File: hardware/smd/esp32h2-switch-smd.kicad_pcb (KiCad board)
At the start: 2 copper layers, 0 parts

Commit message: Complete PCB and schematics after fucking a lot of iterations
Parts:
- added AE1: Antenna_Chip, KiCadX_Antennas_SMD:PCB_antenna_Espressif_2.4GHz_right, F.Cu at (150.5, 112.7)
- added C1: 22u 10V, Capacitor_THT:CP_Radial_D4.0mm_P1.50mm, F.Cu at (162.1, 106.8)
- added C10: 100n 10V X7R, Capacitor_SMD:C_0402_1005Metric, B.Cu at (158.7, 104.3)
- added C11: 100n 35V X7R, Capacitor_SMD:C_0603_1608Metric, B.Cu at (170.0, 96.7)
- added C12: 1n 10V X7R, Capacitor_SMD:C_0402_1005Metric, B.Cu at (158.7, 105.3)
- added C13: 2.2n 35V X7R, Capacitor_SMD:C_0402_1005Metric, B.Cu at (168.7, 93.6)
- added C14: 100n 10V X7R, Capacitor_SMD:C_0402_1005Metric, F.Cu at (156.5, 104.5)
- added C15: 5.6p C0G, Capacitor_SMD:C_0201_0603Metric, F.Cu at (155.1, 108.1)
- added C16: 100n 10V X7R, Capacitor_SMD:C_0402_1005Metric, F.Cu at (156.5, 101.3)
- added C17: 8p 10V C0G, Capacitor_SMD:C_0201_0603Metric, F.Cu at (154.2, 108.2)
- added C18: 2.2p C0G, Capacitor_SMD:C_0201_0603Metric, F.Cu at (155.5, 109.1)
- added C19: 100n 10V X7R, Capacitor_SMD:C_0402_1005Metric, F.Cu at (150.4, 102.2)
- added C2: 100n 10V X7R, Capacitor_SMD:C_0402_1005Metric, F.Cu at (169.9, 105.8)
- added C20: 100n 10V X7R, Capacitor_SMD:C_0402_1005Metric, F.Cu at (152.2, 105.8)
- added C21: 8p 10V C0G, Capacitor_SMD:C_0201_0603Metric, F.Cu at (150.9, 107.4)
- added C22: 100n 10V X7R, Capacitor_SMD:C_0402_1005Metric, F.Cu at (154.3, 106.2)
- added C3: 220n 275V X2, Capacitor_THT:C_Rect_L13.0mm_W6.0mm_P10.00mm_FKS3_FKP3_MKS4, F.Cu at (144.9, 94.8)
- added C4: 4.7u 400V, Capacitor_THT:CP_Radial_D6.3mm_P2.50mm, F.Cu at (164.7, 84.8)
- added C5: 22u 10V, Capacitor_THT:CP_Radial_D4.0mm_P1.50mm, F.Cu at (172.7, 106.9)
- added C6: 100n 10V X7R, Capacitor_SMD:C_0402_1005Metric, F.Cu at (169.9, 107.9)
- added C7: 2.2n 50V X7R, Capacitor_SMD:C_0402_1005Metric, B.Cu at (167.6, 98.1)
- added C8: 470u 10V, KiCadX_Capacitors_THT:CP_Radial_D6.0mm_P2.50mm, F.Cu at (159.1, 84.8)
- added C9: 22u 35V, Capacitor_THT:CP_Radial_D5.0mm_P2.00mm, F.Cu at (173.2, 85.1)
- added D1: 1A 600V, Package_TO_SOT_SMD:TO-269AA, B.Cu at (149.7, 89.5)
- added D2: 40V 1A, Diode_SMD:D_SOD-323, B.Cu at (170.2, 93.6)
- added D3: 40V 1A, Diode_SMD:D_SOD-323, B.Cu at (158.7, 102.2)
- added D4: 40V 1A, Diode_SMD:D_SOD-323, B.Cu at (137.1, 108.5)
- added D5: Blue, 3V, 10mA, LED_SMD:LED_0603_1608Metric, F.Cu at (145.5, 107.4)
- added D6: Red, 2V, 10mA, LED_SMD:LED_0603_1608Metric, F.Cu at (144.1, 107.4)
- added F1: T500mA 250V, Fuse:Fuse_Littelfuse_395Series, F.Cu at (124.7, 85.7)
- added FL1: 2×4.7m ≥0.3A ≤2R, KiCadX_Inductors_THT:TDK_B82720K_Vertical_13x9.5mm_P10x7.5mm, F.Cu at (149.0, 86.5)
- added J1: Screw_Terminal_01x02, TerminalBlock_Phoenix:TerminalBlock_Phoenix_PT-1,5-2-5.0-H_1x02_P5.00mm_Horizontal, F.Cu at (127.3, 90.9)
- added J2: Screw_Terminal_01x02, TerminalBlock_Phoenix:TerminalBlock_Phoenix_PT-1,5-2-5.0-H_1x02_P5.00mm_Horizontal, F.Cu at (127.3, 101.9)
- added J5: UART, Connector_PinHeader_1.27mm:PinHeader_1x04_P1.27mm_Vertical, F.Cu at (147.9, 104.0)
- added J6: Conn_01x02_Pin, Connector_PinHeader_1.27mm:PinHeader_1x02_P1.27mm_Vertical, F.Cu at (147.9, 100.4)
- added K1: SPST, 5V 72R, 10A 250VAC, KiCadX_Relays_THT:Relay_SPST_OJ_SH_105HM_000, F.Cu at (136.8, 100.4)
- added L1: 3.9 nH, Inductor_SMD:L_0402_1005Metric, F.Cu at (155.7, 106.9)
- added NT1: NetTie_2, KiCadX_NetTies:NetTie_2_D0.5_P4.0, B.Cu at (128.9, 88.8)
- added NT2: NetTie_2, KiCadX_NetTies:NetTie_2_D0.5_P4.0, B.Cu at (121.7, 97.0)
- added Q1: NPN, 40V, 500mA, Package_TO_SOT_SMD:SOT-323_SC-70, F.Cu at (143.7, 104.2)
- added R1: 30k, Resistor_SMD:R_0402_1005Metric, B.Cu at (168.7, 95.7)
- added R10: 10k, Resistor_SMD:R_0402_1005Metric, F.Cu at (150.4, 100.8)
- added R2: 470R, Resistor_SMD:R_0402_1005Metric, B.Cu at (161.8, 104.8)
- added R3: 10k, Resistor_SMD:R_0402_1005Metric, B.Cu at (163.8, 106.1)
- added R4: 10k, Resistor_SMD:R_0402_1005Metric, B.Cu at (165.6, 106.1)
- added R5: 330R, Resistor_SMD:R_0402_1005Metric, F.Cu at (142.9, 106.9)
- added R6: 220R, Resistor_SMD:R_0402_1005Metric, F.Cu at (145.5, 105.0)
- added R7: 10k, Resistor_SMD:R_0402_1005Metric, F.Cu at (154.7, 99.9)
- added R8: 330R, Resistor_SMD:R_0402_1005Metric, F.Cu at (143.9, 102.1)
- added R9: 10k, Resistor_SMD:R_0402_1005Metric, F.Cu at (145.5, 103.2)
- added RV1: 275V, Varistor:RV_Disc_D9mm_W4.4mm_P5mm, F.Cu at (133.2, 88.7)
- added T1: Wurth 750370423, KiCadX_Transformers_THT:Wurth_750370423_THT_E13, F.Cu at (166.6, 96.5)
- added TH1: 10R 25C, KiCadX_Thermistors_THT:NTC10D_7_Disc_D7.0mm_P5.0mm, F.Cu at (139.5, 86.3)
- added U1: LM1117F-3.3, Package_TO_SOT_SMD:SOT-89-3, F.Cu at (166.6, 107.4)
- added U2: VIPER06, KiCadX_ACDC_Converters_SMD:VIPER06_SSO10, B.Cu at (164.1, 95.2)
- added U3: EL3H7, Package_SO:SSOP-4_4.4x2.6mm_P1.27mm, B.Cu at (167.0, 104.1)
- added U4: TL431, Package_TO_SOT_SMD:SOT-23, B.Cu at (167.5, 107.5)
- added U5: ESP32-H2, KiCadX_MCU_Espressif:TQFN_32_1EP_4x4mm_P0.4mm_EP2.4x2.4mm_Compact, F.Cu at (153.6, 102.8)
- added Y1: 32MHz ±10ppm CL8pF, Crystal:Crystal_SMD_2016-4Pin_2.0x1.6mm, F.Cu at (152.5, 107.8)
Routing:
- net +5V: track 0.00 -> 80.3 mm, vias 0 -> 1
- net N: track 0.00 -> 54.3 mm
- net GND: track 0.00 -> 33.4 mm, vias 0 -> 53
- net L: track 0.00 -> 26.7 mm
- net GND_P: track 0.00 -> 26.4 mm
- net /Power supply/VRECT: track 0.00 -> 25.4 mm
- net /N_IN: track 0.00 -> 17.4 mm
- net Net-(D2-K): track 0.00 -> 17.3 mm
- net L_OUT: track 0.00 -> 15.6 mm
- net +3.3V: track 0.00 -> 15.3 mm, vias 0 -> 16
- net /Control unit/RELAY_CTRL: track 0.00 -> 10.9 mm, vias 0 -> 2
- net /Control unit/RELAY_COIL: track 0.00 -> 9.88 mm
- net Net-(U2-COMP): track 0.00 -> 9.32 mm
- net /Control unit/LED_RUN: track 0.00 -> 8.21 mm, vias 0 -> 2
- net BOOT: track 0.00 -> 7.55 mm
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- added copper zone on In2.Cu, net +3.3V
- added copper zone on B.Cu, net /Power supply/DRAIN
- added copper zone on B.Cu, net GND
- added copper zone on F.Cu, net GND
- added copper zone on In1.Cu, net GND
- added copper zone on B.Cu, net GND_P
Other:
- board outline added: 54.6 x 34.2 mm
- copper layers 2 -> 4

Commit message: Relink symbols and footprints to new lib and fix few errors
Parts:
- AE1: footprint KiCadX_Antennas_SMD:PCB_antenna_Espressif_2.4GHz_right -> PCM_SKC_Antennas_SMD:Antenna_PCB_Espressif_2.4GHz_Right
- C8: footprint KiCadX_Capacitors_THT:CP_Radial_D6.0mm_P2.50mm -> PCM_SKC_Capacitors_THT:CP_Radial_D6.0mm_P2.50mm
- FL1: footprint KiCadX_Inductors_THT:TDK_B82720K_Vertical_13x9.5mm_P10x7.5mm -> PCM_SKC_Inductors_THT:TDK_B82720K_Vertical_13x9.5mm_P10x7.5mm
- K1: footprint KiCadX_Relays_THT:Relay_SPST_OJ_SH_105HM_000 -> PCM_SKC_Relays_THT:OJ_SH_105HM_SPST
- NT1, NT2: footprint KiCadX_NetTies:NetTie_2_D0.5_P4.0 -> PCM_SKC_NetTies:NetTie_2_D0.5_P4.0
- T1: footprint KiCadX_Transformers_THT:Wurth_750370423_THT_E13 -> PCM_SKC_Transformers_THT:Wurth_750370423_THT_E13
- TH1: footprint KiCadX_Thermistors_THT:NTC10D_7_Disc_D7.0mm_P5.0mm -> PCM_SKC_Thermistors_THT:NTC10D_7_Disc_D7.0mm_P5.0mm
- U2: footprint KiCadX_ACDC_Converters_SMD:VIPER06_SSO10 -> PCM_SKC_ACDC_Converters_SMD:STMicroelectronics_VIPER06_SSO10
- U5: footprint KiCadX_MCU_Espressif:TQFN_32_1EP_4x4mm_P0.4mm_EP2.4x2.4mm_Compact -> PCM_SKC_MCU_Espressif:TQFN_32_1EP_4x4mm_P0.4mm_EP2.4x2.4mm_Compact

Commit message: Added logo on silkscreen
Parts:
- added REF**: SIVAKOV_TECH_Circle_Medium_D13.22_1, SIVAKOV.TECH:SIVAKOV_TECH_Circle_Medium_D13.22_1, B.Cu at (135.5, 100.9)

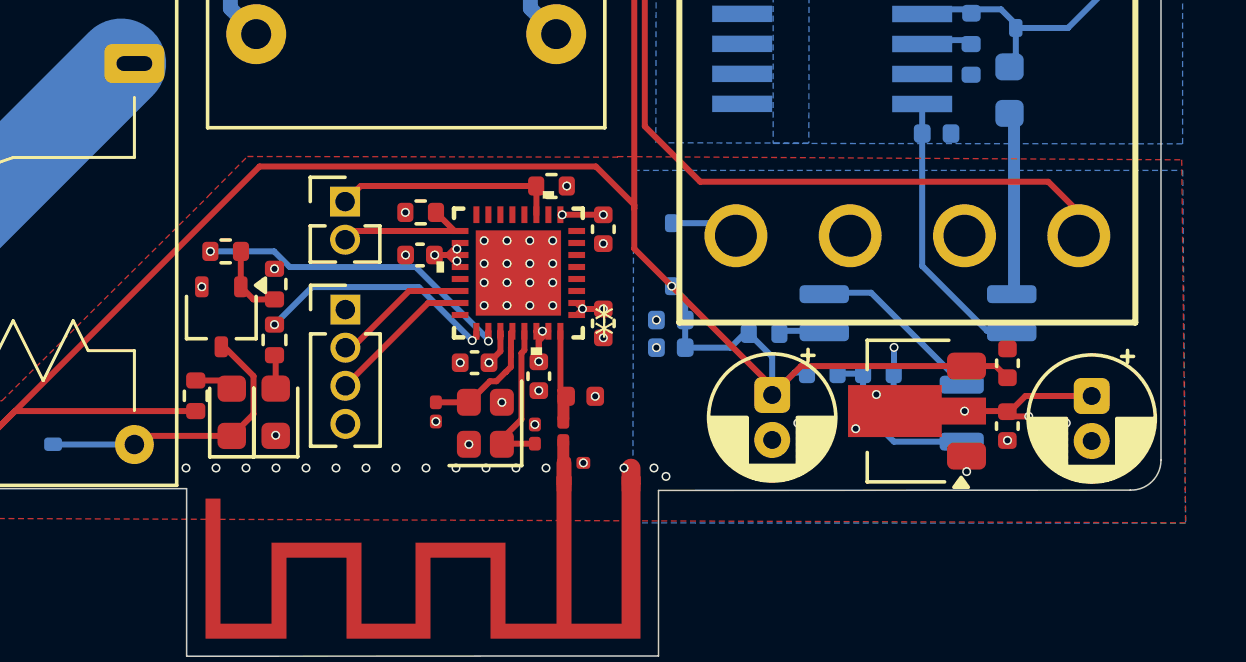
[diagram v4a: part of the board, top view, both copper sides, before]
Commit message: Make vias a bit bigger because of JLCPCB prices and change out-of-stock component
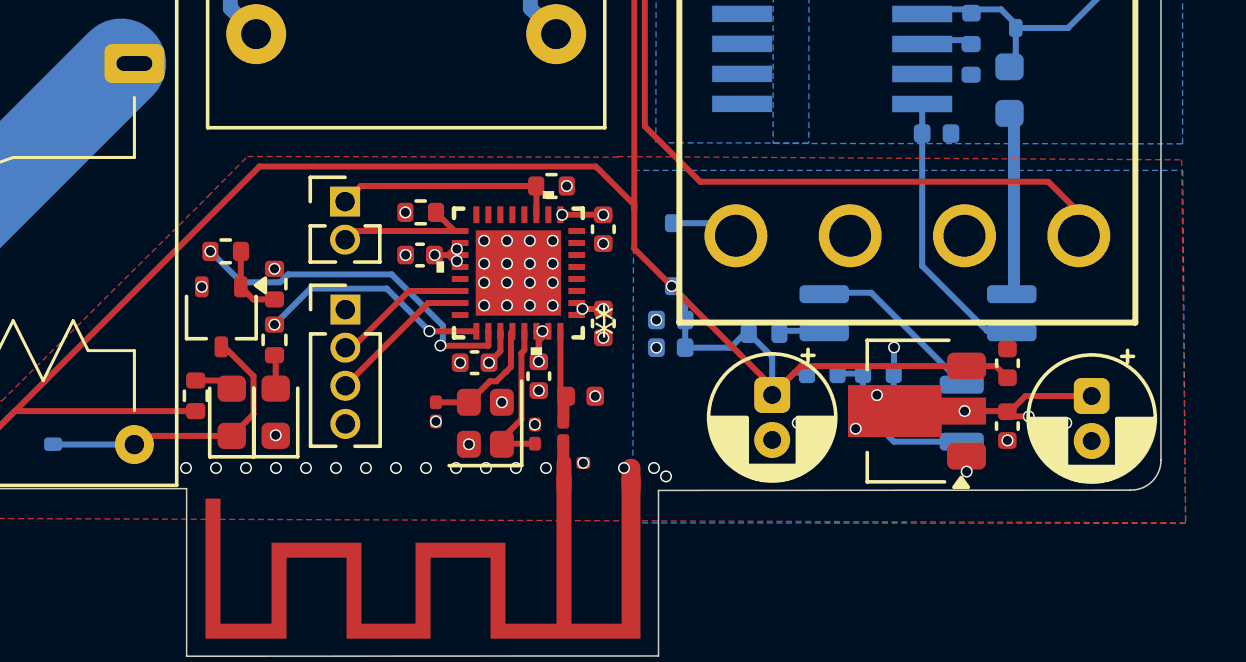
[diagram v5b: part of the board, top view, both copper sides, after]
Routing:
- net /Control unit/RELAY_CTRL: track 10.9 -> 11.8 mm

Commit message: Add a user layer with pinout
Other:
- board text added: "+3.3V"
- board text added: "BOOT"
- board text added: "GND"
- board text added: "LED_RELAY"
- board text added: "LED_RUN"
- board text added: "L_IN"
- board text added: "L_OUT"
- board text added: "N_IN"
- board text added: "N_OUT"
- board text added: "RESET"
- board text added: "RX"
- board text added: "TX"
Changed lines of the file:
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@@
 		)
+	)
+	(gr_rect
+		(start 144.81 105.96)
+		(end 146.27 108.91)
+		(stroke
+			(width 0.05)
+			(type default)
+		)
+		(fill no)
+		(layer "Dwgs.User")
+	)
+	(gr_rect
+		(start 147.28 99.82)
+		(end 148.44 100.98)
+		(stroke
+			(width 0.05)
+			(type default)
+		)
+		(fill no)
+		(layer "Dwgs.User")
+	)
+	(gr_circle
+		(center 147.87 106.54)
+		(end 148.37 106.25)
+		(stroke
+			(width 0.05)
+			(type default)
+		)
+		(fill no)
+		(layer "Dwgs.User")
+	)
+	(gr_circle
+		(center 147.87 105.27)
+		(end 148.37 104.98)
+		(stroke
+			(width 0.05)
+			(type default)
+		)
+		(fill no)
+		(layer "Dwgs.User")
+	)
+	(gr_rect
+		(start 143.35 105.96)
+		(end 144.81 108.91)
+		(stroke
+			(width 0.05)
+			(type default)
+		)
+		(fill no)
+		(layer "Dwgs.User")
+	)
+	(gr_rect
+		(start 147.29 103.42)
+		(end 148.45 104.58)
+		(stroke
+			(width 0.05)
+			(type default)
+		)
+		(fill no)
+		(layer "Dwgs.User")
+	)
+	(gr_circle
+		(center 147.86 101.67)
+		(end 148.36 101.38)
+		(stroke
+			(width 0.05)
+			(type default)
+		)
+		(fill no)
+		(layer "Dwgs.User")
+	)
+	(gr_circle
+		(center 147.87 107.81)
+		(end 148.37 107.52)
+		(stroke
+			(width 0.05)
+			(type default)
+		)
+		(fill no)
+		(layer "Dwgs.User")
 	)
 	(gr_line
@@
 		(layer "Edge.Cuts")
 	)
+	(gr_text "LED_RELAY"
+		(at 144.61 109.44 90)
+		(layer "Dwgs.User")
+		(effects
+			(font
+				(size 1 1)
+				(thickness 0.1)
+			)
+			(justify right bottom)
+		)
+	)
+	(gr_text "+3.3V"
+		(at 148.438014 104.58 0)
+		(layer "Dwgs.User")
+		(effects
+			(font
+				(size 1 1)
+				(thickness 0.1)
+			)
+			(justify left bottom)
+		)
+	)
+	(gr_text "N_IN"
+		(at 125.24 96.63 0)
+		(layer "Dwgs.User")
+		(effects
+			(font
+				(size 1.5 1.5)
+				(thickness 0.15)
+			)
+			(justify right bottom)
+		)
+	)
+	(gr_text "N_OUT"
+		(at 125.24 107.59 0)
+		(layer "Dwgs.User")
+		(effects
+			(font
+				(size 1.5 1.5)
+				(thickness 0.15)
+			)
+			(justify right bottom)
+		)
+	)
+	(gr_text "L_IN"
+		(at 125.24 91.59 0)
+		(layer "Dwgs.User")
+		(effects
+			(font
+				(size 1.5 1.5)
+				(thickness 0.15)
+			)
+			(justify right bottom)
+		)
+	)
+	(gr_text "BOOT"
+		(at 148.44 100.98 0)
+		(layer "Dwgs.User")
+		(effects
+			(font
+				(size 1 1)
+				(thickness 0.1)
+			)
+			(justify left bottom)
+		)
+	)
+	(gr_text "GND"
+		(at 148.438014 108.39 0)
+		(layer "Dwgs.User")
+		(effects
+			(font
+				(size 1 1)
+				(thickness 0.1)
+			)
+			(justify left bottom)
+		)
+	)
+	(gr_text "RX"
+		(at 148.438014 107.12 0)
+		(layer "Dwgs.User")
+		(effects
+			(font
+				(size 1 1)
+				(thickness 0.1)
+			)
+			(justify left bottom)
+		)
+	)
+	(gr_text "L_OUT"
+		(at 125.24 102.55 0)
+		(layer "Dwgs.User")
+		(effects
+			(font
+				(size 1.5 1.5)
+				(thickness 0.15)
+			)
+			(justify right bottom)
+		)
+	)
+	(gr_text "TX"
+		(at 148.438014 105.85 0)
+		(layer "Dwgs.User")
+		(effects
+			(font
+				(size 1 1)
+				(thickness 0.1)
+			)
+			(justify left bottom)
+		)
+	)
+	(gr_text "RESET"
+		(at 148.45 102.248014 0)
+		(layer "Dwgs.User")
+		(effects
+			(font
+				(size 1 1)
+				(thickness 0.1)
+			)
+			(justify left bottom)
+		)
+	)
+	(gr_text "LED_RUN"
+		(at 146.26 109.42 90)
+		(layer "Dwgs.User")
+		(effects
+			(font
+				(size 1 1)
+				(thickness 0.1)
+			)
+			(justify right bottom)
+		)
+	)
 	(segment
